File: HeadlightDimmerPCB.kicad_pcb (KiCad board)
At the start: 2 copper layers, 27 x 14 mm, 12 parts, among them J1 Conn_02x02_Counter_Clockwise, Q1 NMOS, U1 LMC555xM

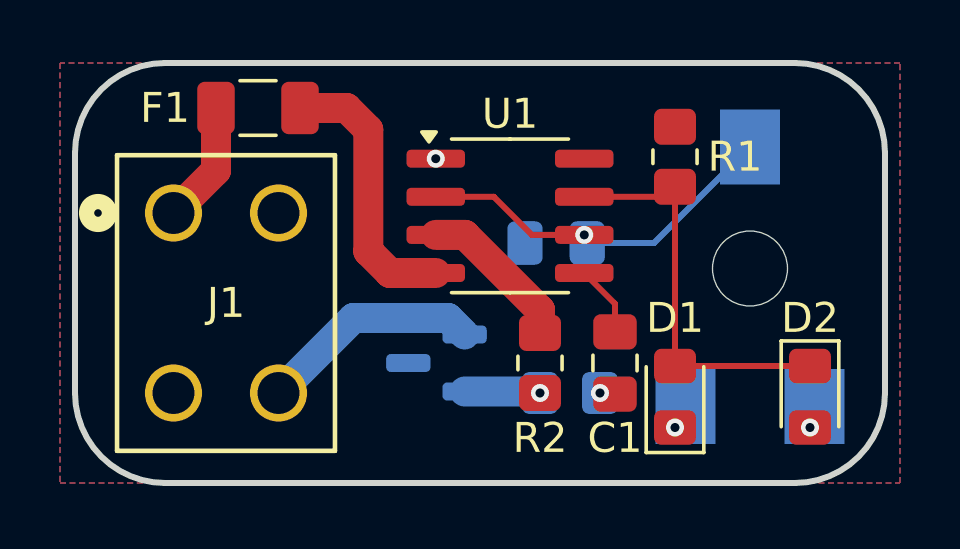
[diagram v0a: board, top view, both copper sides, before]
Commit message: more routing and part selection
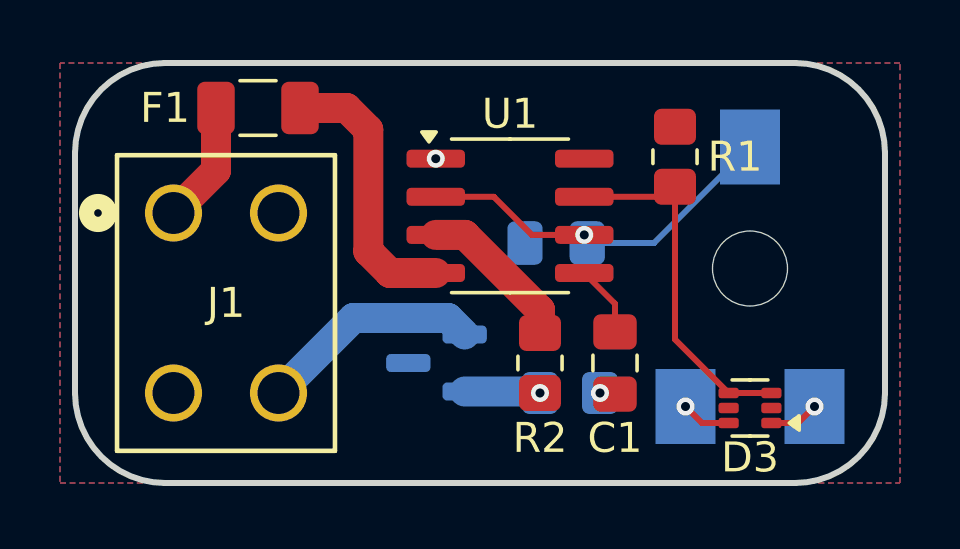
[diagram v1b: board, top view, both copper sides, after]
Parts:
- removed D1, D2: D, Diode_SMD:D_0805_2012Metric_Pad1.15x1.40mm_HandSolder
- added D3: BAT54V-7, Package_TO_SOT_SMD:SOT-563, F.Cu at (164.5, 94.5)
- R2: value 100 -> 1K
- R3, RV1: value 10k -> 10K
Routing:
- net /DIS: track 13.6 -> 12.2 mm
- net Net-(D3-A1): track 0.76 -> 1.67 mm
- net Net-(D3-C1): track 0.84 -> 1.67 mm
